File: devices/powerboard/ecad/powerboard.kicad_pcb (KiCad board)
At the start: 2 copper layers, 100 x 55 mm, 40 parts, among them J1 Conn_02x02_Top_Bottom, J10 Conn_02x01, J2 Conn_02x02_Top_Bottom, J3 Conn_02x01, J4 Conn_02x01, J5 USB_A, J6 JST PH, J7 JST PH, J8 47053-1000, J9 USB_A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

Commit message: [WIP][powerboard] changes the inductor
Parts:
- added C12: DNF, Capacitor_SMD:C_1206_3216Metric, F.Cu at (94.1, 87.5)
- added C13: DNF, Capacitor_SMD:C_1206_3216Metric, F.Cu at (94.1, 90.8)
- L1: footprint common:L_Bourns_SRP1270_13.7x13.7mm -> common:L_Bourns_SRP6050CA_6.6x6.4mm
- moved C5 6.04 mm to (142.5, 84.6)
- moved L1 5.10 mm to (144.9, 89.0)
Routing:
- net /SW: track 14.2 -> 0.00 mm
- net +5V: track 104.0 -> 90.0 mm
- net /VBOOT: track 10.5 -> 0.00 mm

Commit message: Powerboard revA done
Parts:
- added C14: DNF, Capacitor_SMD:C_0603_1608Metric, F.Cu at (166.6, 91.8)
- added REF**: OSHW-Logo2_9.8x8mm_SilkScreen, Symbol:OSHW-Logo2_9.8x8mm_SilkScreen, F.Cu at (170.2, 55.3)
- J1, J2: footprint Connector_Molex:Molex_Mini-Fit_Jr_5569-04A2_2x02_P4.20mm_Horizontal -> common:Molex_Mini-Fit_Jr_5569-04A2_2x02_P4.20mm_Horizontal
- J10, J3, J4: footprint Connector_Molex:Molex_Mini-Fit_Jr_5569-02A2_2x01_P4.20mm_Horizontal -> common:Molex_Mini-Fit_Jr_5569-02A2_2x01_P4.20mm_Horizontal
- moved C13 42.6 mm to (136.7, 89.0), turned to -90 degrees
- moved C12 40.2 mm to (134.3, 89.0), turned to -90 degrees
- moved Q2 12.2 mm to (148.9, 80.9)
- moved C10 8.76 mm to (147.7, 92.6)
- moved R3 8.72 mm to (145.9, 92.8)
- moved R4 8.72 mm to (143.9, 92.8)
- moved J8 7.92 mm to (104.0, 64.7), turned to -90 degrees
- moved C4 7.73 mm to (147.9, 84.6)
- moved D1 7.73 mm to (144.9, 80.9)
- moved R1 7.73 mm to (141.9, 81.8)
- moved R2 7.73 mm to (145.9, 84.4)
- moved C1 7.72 mm to (139.1, 89.0)
- moved C2 7.72 mm to (141.5, 89.0)
- moved C3 7.72 mm to (143.5, 89.0)
- moved C5 7.72 mm to (150.2, 84.6)
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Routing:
- net GND: track 64.4 -> 86.8 mm, vias 77 -> 113
- net /DP: track 35.1 -> 52.0 mm
- net +12V: track 56.8 -> 73.1 mm
- net /DN: track 33.0 -> 47.9 mm
- net +5V: track 90.0 -> 95.2 mm
- net /TACHO: track 29.3 -> 25.7 mm
- net /FAN: track 21.3 -> 19.9 mm
- net /FB: track 6.80 -> 5.78 mm
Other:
- board text added: "5V 8A Max"
- board text added: "6 - 24V"
- board text added: "FAN"
- board text added: "PC FAN"
- board text added: "Plug Only If VIN=12V"
- board text added: "TACHO"
- board text added: "VIN GND"
- board text added: "ZACI Powerboard rev A"

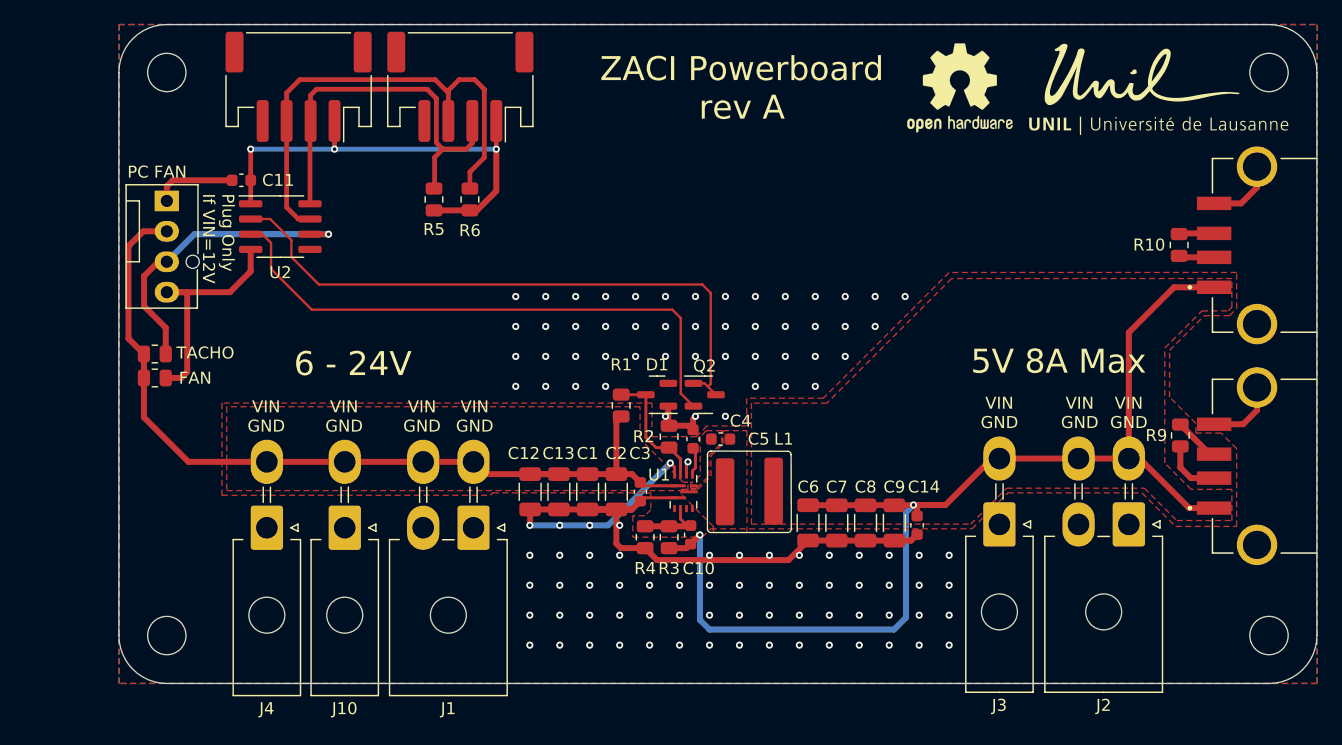
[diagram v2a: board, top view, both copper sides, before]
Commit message: Updates power distribution board
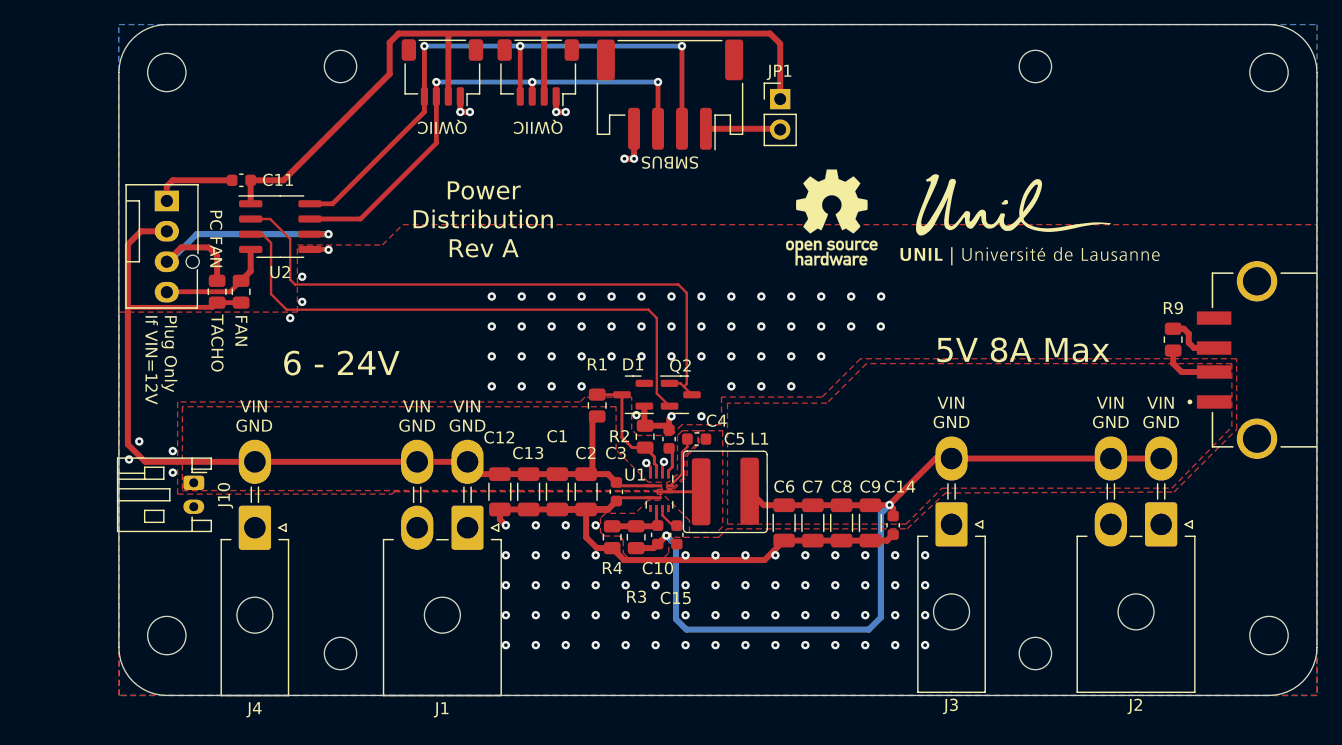
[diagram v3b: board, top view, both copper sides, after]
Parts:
- removed R10: 100, Resistor_SMD:R_0805_2012Metric
- removed R5, R6: 10k, Resistor_SMD:R_0805_2012Metric
- removed the REF** at (170.2, 55.3)
- added C15: 56n, Capacitor_SMD:C_0603_1608Metric, F.Cu at (146.6, 92.6)
- added JP1: Jumper_2_Open, Connector_PinHeader_2.54mm:PinHeader_1x02_P2.54mm_Vertical, F.Cu at (155.2, 56.2)
- added REF**: MountingHole_2.7mm_M2.5, MountingHole:MountingHole_2.7mm_M2.5, F.Cu at (118.5, 53.5)
- added REF**: OSHW-Logo_7.5x8mm_SilkScreen, Symbol:OSHW-Logo_7.5x8mm_SilkScreen, F.Cu at (159.5, 66.1)
- added REF**1: MountingHole_2.7mm_M2.5, MountingHole:MountingHole_2.7mm_M2.5, F.Cu at (176.5, 53.5)
- added REF**2: MountingHole_2.7mm_M2.5, MountingHole:MountingHole_2.7mm_M2.5, F.Cu at (118.5, 102.5)
- added REF**3: MountingHole_2.7mm_M2.5, MountingHole:MountingHole_2.7mm_M2.5, F.Cu at (176.5, 102.5)
- J10: value Conn_02x01 -> S2B-PH-K; footprint common:Molex_Mini-Fit_Jr_5569-02A2_2x01_P4.20mm_Horizontal -> Connector_JST:JST_PH_S2B-PH-K_1x02_P2.00mm_Horizontal
- J6, J7: value JST PH -> SM04-SRSS-TB; footprint common:JST_PH_S4B-PH-SM4-TB_1x04-1MP_P2.00mm_Horizontal -> common:JST_SH_SM04B-SRSS-TB_1x04-1MP_P1.00mm_Horizontal
- J9: value USB_A -> S4B-PH-SM4-TB; footprint common:AMP_87583-2010RPLF -> common:JST_PH_S4B-PH-SM4-TB_1x04-1MP_P2.00mm_Horizontal
- moved J9 50.6 mm to (146.0, 55.9), turned to 180 degrees
- moved J10 13.1 mm to (106.2, 88.2), turned to -90 degrees
- moved J7 12.1 mm to (127.0, 54.0)
- moved R8 10.2 mm to (110.2, 72.3), turned to 90 degrees
- moved J5 8.86 mm to (195.0, 78.0)
- moved R9 8.02 mm to (188.0, 76.3)
- moved R7 7.35 mm to (108.2, 72.3), turned to 90 degrees
- moved J6 6.61 mm to (135.0, 54.0)
- moved J3 4.00 mm to (169.5, 91.7)
- moved C10 2.75 mm to (145.0, 92.6)
- moved R3 2.75 mm to (143.2, 92.8)
- moved R4 2.75 mm to (141.2, 92.8)
- moved J2 2.70 mm to (187.0, 91.7)
- moved C1 2.53 mm to (136.6, 89.0)
- moved C13 2.53 mm to (134.2, 89.0)
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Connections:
- J10 pad 1: GND -> +12V
- J10 pad 2: +12V -> GND
- J6 pad 1: +3V3 -> GND
- J6 pad 2: /SCL -> +3V3
- J6 pad 4: GND -> /SCL
- J7 pad 1: +3V3 -> GND
- J7 pad 2: /SCL -> +3V3
- J7 pad 4: GND -> /SCL
- J9 pad 1: +5V -> Net-(J9-Pin_1)
- J9 pad 2: Net-(J9-D-) -> /SCL
- J9 pad 3: Net-(J9-D+) -> /SDA
- U1 pad 5: unconnected-(U1-SS-Pad5) -> Net-(U1-SS)
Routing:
- net +3V3: track 39.5 -> 68.2 mm, vias 3 -> 0
- net +5V: track 95.2 -> 75.4 mm
- net /SCL: track 32.8 -> 50.8 mm, vias 0 -> 3
- net GND: track 86.8 -> 71.6 mm, vias 113 -> 128
- net /FAN: track 19.9 -> 9.54 mm
- net +12V: track 73.1 -> 80.3 mm
- net Net-(J9-Pin_1): track 0.00 -> 6.21 mm
- net /VBOOT: track 0.00 -> 4.49 mm
- net /SW: track 0.00 -> 2.97 mm
- net Net-(J9-D-): track 2.97 -> 0.00 mm
- net Net-(J9-D+): track 2.94 -> 0.00 mm
- net /TACHO: track 25.7 -> 23.1 mm
- net Net-(U1-SS): track 0.00 -> 2.13 mm
- net /DP: track 52.0 -> 51.1 mm
- net /DN: track 47.9 -> 47.1 mm
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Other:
- board size 100 x 55 mm -> 100 x 56 mm
- board text added: "Power Distribution Rev A"
- board text added: "QWIIC"
- board text added: "SMBUS"
- board text removed: "ZACI Powerboard rev A"

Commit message: Conforms all board together
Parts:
- C12, C13: value DNF -> 22u
- C14: value DNF -> 100n
- moved REF** 15.0 mm to (144.6, 68.0)
- moved C10 4.51 mm to (146.3, 96.9)
- moved C15 4.51 mm to (147.9, 96.9)
- moved R3 4.51 mm to (144.5, 97.1)
- moved R4 4.51 mm to (142.5, 97.1)
- moved C1 1.50 mm to (138.1, 89.0)
- moved C12 1.50 mm to (133.3, 89.0)
- moved C13 1.50 mm to (135.7, 89.0)
- moved C2 1.50 mm to (140.5, 89.0)
- moved C3 1.00 mm to (142.5, 89.0)
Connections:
- net Net-(U1-SS) renamed /BOOT
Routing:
- net GND: track 71.6 -> 78.3 mm, vias 128 -> 130
- net +5V: track 75.4 -> 69.1 mm
- net /BOOT: track 2.13 -> 7.48 mm
- net /SW: track 2.97 -> 7.54 mm
- net /FB: track 5.28 -> 9.55 mm
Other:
- board text added: "5V 8A max"
- board text added: "Power Distribution rev A"
- board text added: "Power Up SMBUS"
- board text removed: "5V 8A Max"
- board text removed: "Power Distribution Rev A"
